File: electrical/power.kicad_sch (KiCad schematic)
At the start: 58 parts

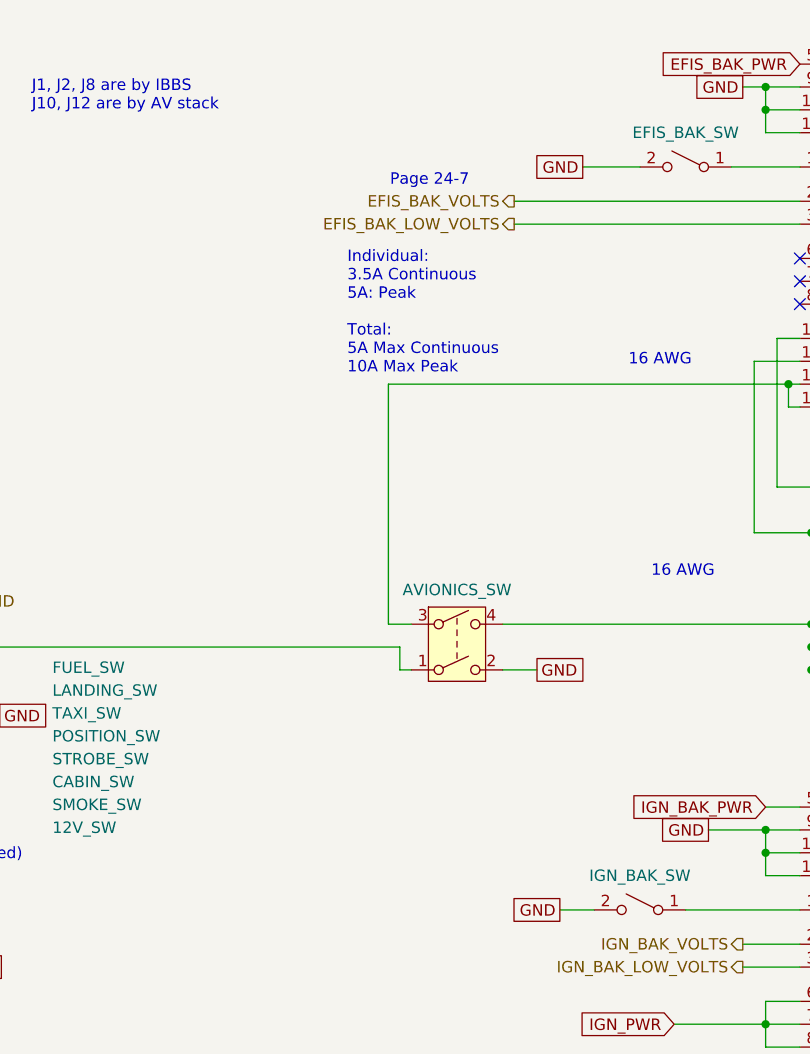
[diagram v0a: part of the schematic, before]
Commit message: Added switch numbers.
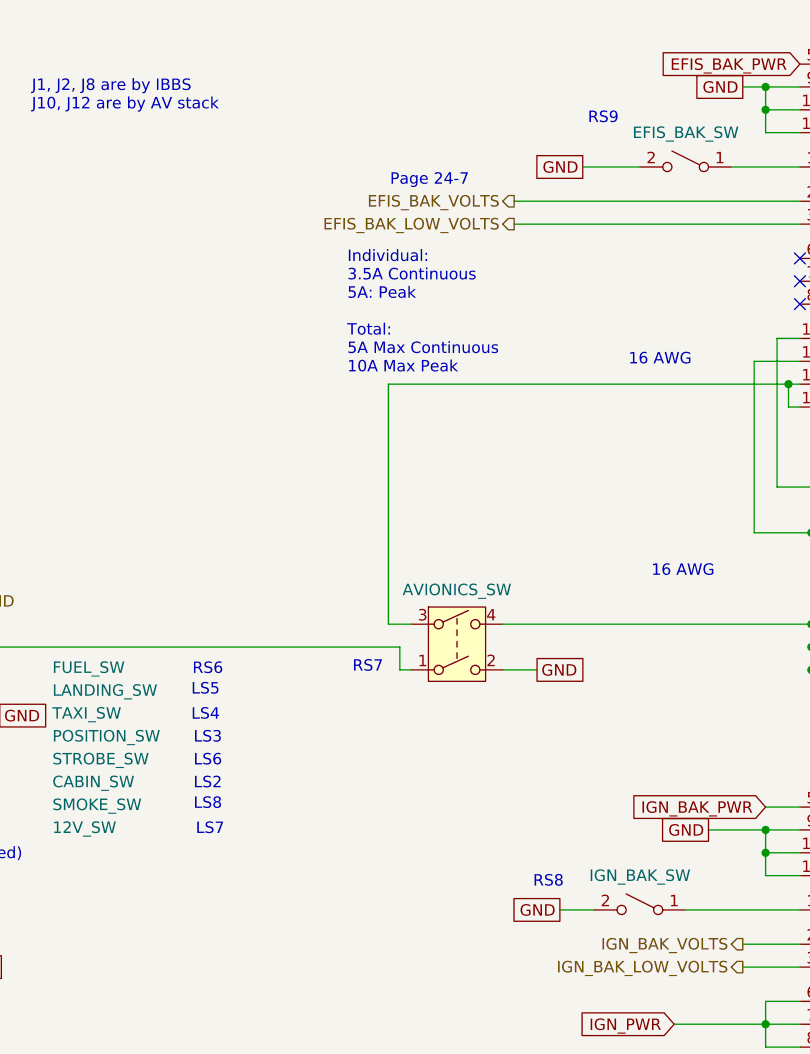
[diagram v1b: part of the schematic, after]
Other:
- note added: "LS2"
- note added: "LS3"
- note added: "LS4"
- note added: "LS5"
- note added: "LS6"
- note added: "LS7"
- note added: "LS8"
- note added: "RS6"
- note added: "RS7"
- note added: "RS8"
- note added: "RS9"
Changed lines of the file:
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@@
 	(title_block
 		(title "Power Distribution")
-		(date "2025-10-01")
-		(rev "1.1.2")
+		(date "2025-10-02")
+		(rev "1.1.3")
 		(company "N78HR")
 	)
@@
 		)
 	)
+	(text "RS8"
+		(exclude_from_sim no)
+		(at 138.43 108.712 0)
+		(effects
+			(font
+				(size 1.27 1.27)
+			)
+		)
+	)
 	(text "Power/Ground 20 AWG\nSignals 22 AWG\nUnless Noted"
 		(exclude_from_sim no)
@@
 		)
 	)
+	(text "RS6"
+		(exclude_from_sim no)
+		(at 100.584 85.09 0)
+		(effects
+			(font
+				(size 1.27 1.27)
+			)
+		)
+	)
 	(text "2A"
 		(exclude_from_sim no)
@@
 		)
 	)
+	(text "LS3"
+		(exclude_from_sim no)
+		(at 100.584 92.71 0)
+		(effects
+			(font
+				(size 1.27 1.27)
+			)
+		)
+	)
 	(text "Backup"
 		(exclude_from_sim no)
@@
 		)
 	)
+	(text "LS4"
+		(exclude_from_sim no)
+		(at 100.33 90.17 0)
+		(effects
+			(font
+				(size 1.27 1.27)
+			)
+		)
+	)
 	(text "16 AWG"
 		(exclude_from_sim no)
@@
 		)
 	)
+	(text "LS7"
+		(exclude_from_sim no)
+		(at 100.838 102.87 0)
+		(effects
+			(font
+				(size 1.27 1.27)
+			)
+		)
+	)
+	(text "RS9"
+		(exclude_from_sim no)
+		(at 144.526 23.876 0)
+		(effects
+			(font
+				(size 1.27 1.27)
+			)
+		)
+	)
 	(text "14 AWG"
 		(exclude_from_sim no)
@@
 		)
 	)
+	(text "LS5"
+		(exclude_from_sim no)
+		(at 100.33 87.376 0)
+		(effects
+			(font
+				(size 1.27 1.27)
+			)
+		)
+	)
 	(text "16 AWG"
 		(exclude_from_sim no)
@@
 		)
 	)
+	(text "LS2"
+		(exclude_from_sim no)
+		(at 100.584 97.79 0)
+		(effects
+			(font
+				(size 1.27 1.27)
+			)
+		)
+	)
 	(text "13A"
 		(exclude_from_sim no)
@@
 		)
 	)
+	(text "RS7"
+		(exclude_from_sim no)
+		(at 118.364 84.836 0)
+		(effects
+			(font
+				(size 1.27 1.27)
+			)
+		)
+	)
 	(text "5A"
 		(exclude_from_sim no)
@@
 		)
 	)
+	(text "LS8"
+		(exclude_from_sim no)
+		(at 100.584 100.076 0)
+		(effects
+			(font
+				(size 1.27 1.27)
+			)
+		)
+	)
 	(text "GROUND_BLOCK"
 		(exclude_from_sim no)
@@
 		(effects
 			(font
+				(size 1.27 1.27)
+			)
+		)
+	)
+	(text "LS6"
+		(exclude_from_sim no)
+		(at 100.584 95.25 0)
+		(effects
+			(font

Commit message: Added RS232 and Canbus wiring notation
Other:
- note added: "Black"
- note added: "Blue"
- note added: "Brown"
- note added: "Destination Open Shield"
- note added: "Green"
- note added: "Pink"
- note added: "Purple"
- note added: "Red"
- note added: "White"
- note added: "White/Black"
- note added: "White/Blue"
- note added: "White/Green"
- note added: "White/Grey"
- note added: "White/Orange"
- note added: "White/Purple"
- note added: "White/Yellow"
- note added: "Yellow"
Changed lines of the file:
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@@
 		(title "Power Distribution")
 		(date "2025-10-02")
-		(rev "1.1.3")
+		(rev "1.1.4")
 		(company "N78HR")
 	)
@@
 		)
 	)
+	(text "Destination\nOpen Shield"
+		(exclude_from_sim no)
+		(at 88.9 74.93 0)
+		(effects
+			(font
+				(size 1.27 1.27)
+			)
+		)
+	)
 	(text "14 AWG"
 		(exclude_from_sim no)
@@
 		)
 	)
+	(text "Yellow"
+		(exclude_from_sim no)
+		(at 92.456 288.798 0)
+		(effects
+			(font
+				(size 1.27 1.27)
+			)
+		)
+	)
 	(text "16 AWG"
 		(exclude_from_sim no)
@@
 		)
 	)
+	(text "Pink"
+		(exclude_from_sim no)
+		(at 92.456 291.084 0)
+		(effects
+			(font
+				(size 1.27 1.27)
+			)
+		)
+	)
 	(text "Pitot Heat (Reserved)"
 		(exclude_from_sim no)
@@
 		)
 	)
+	(text "White/Grey"
+		(exclude_from_sim no)
+		(at 17.78 293.116 0)
+		(effects
+			(font
+				(size 1.27 1.27)
+			)
+		)
+	)
+	(text "White/Purple"
+		(exclude_from_sim no)
+		(at 19.304 285.75 0)
+		(effects
+			(font
+				(size 1.27 1.27)
+			)
+		)
+	)
 	(text "14 AWG"
 		(exclude_from_sim no)
@@
 		)
 	)
+	(text "Blue"
+		(exclude_from_sim no)
+		(at 91.44 280.416 0)
+		(effects
+			(font
+				(size 1.27 1.27)
+			)
+		)
+	)
 	(text "14 AWG"
 		(exclude_from_sim no)
@@
 		)
 	)
+	(text "White/Black"
+		(exclude_from_sim no)
+		(at 19.558 278.13 0)
+		(effects
+			(font
+				(size 1.27 1.27)
+			)
+		)
+	)
 	(text "RS7"
 		(exclude_from_sim no)
@@
 		)
 	)
+	(text "White"
+		(exclude_from_sim no)
+		(at 92.71 296.418 0)
+		(effects
+			(font
+				(size 1.27 1.27)
+			)
+		)
+	)
 	(text "15A"
 		(exclude_from_sim no)
@@
 		)
 	)
+	(text "Purple"
+		(exclude_from_sim no)
+		(at 92.456 286.258 0)
+		(effects
+			(font
+				(size 1.27 1.27)
+			)
+		)
+	)
 	(text "2A"
 		(exclude_from_sim no)
@@
 		)
 	)
+	(text "Brown"
+		(exclude_from_sim no)
+		(at 92.456 293.624 0)
+		(effects
+			(font
+				(size 1.27 1.27)
+			)
+		)
+	)
+	(text "White/Blue"
+		(exclude_from_sim no)
+		(at 19.05 280.416 0)
+		(effects
+			(font
+				(size 1.27 1.27)
+			)
+		)
+	)
+	(text "Red"
+		(exclude_from_sim no)
+		(at 92.456 298.958 0)
+		(effects
+			(font
+				(size 1.27 1.27)
+			)
+		)
+	)
+	(text "Green"
+		(exclude_from_sim no)
+		(at 92.202 283.21 0)
+		(effects
+			(font
+				(size 1.27 1.27)
+			)
+		)
+	)
 	(text "Avionics\nBackup"
 		(exclude_from_sim no)
@@
 		)
 	)
+	(text "White/Yellow"
+		(exclude_from_sim no)
+		(at 19.05 288.29 0)
+		(effects
+			(font
+				(size 1.27 1.27)
+			)
+		)
+	)
+	(text "White/Orange"
+		(exclude_from_sim no)
+		(at 19.05 290.83 0)
+		(effects
+			(font
+				(size 1.27 1.27)
+			)
+		)
+	)
 	(text "5A"
 		(exclude_from_sim no)
@@
 		)
 	)
+	(text "Black"
+		(exclude_from_sim no)
+		(at 91.694 277.876 0)
+		(effects
+			(font
+				(size 1.27 1.27)
+			)
+		)
+	)
 	(text "5A"
 		(exclude_from_sim no)
@@
 		(effects
 			(font
+				(size 1.27 1.27)
+			)
+		)
+	)
+	(text "White"
+		(exclude_from_sim no)
+		(at 18.034 295.402 0)
+		(effects
+			(font
+				(size 1.27 1.27)
+			)
+		)
+	)
+	(text "White/Green"
+		(exclude_from_sim no)
+		(at 19.558 282.956 0)
+		(effects
+			(font

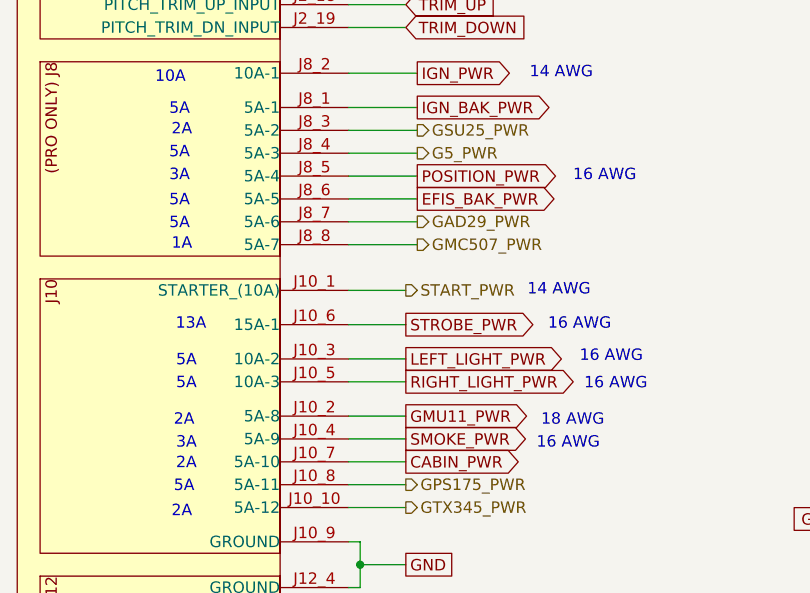
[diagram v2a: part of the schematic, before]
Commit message: Added colors to GTP 59 symbol. Moved power around as best as I could to accomodate lights together.
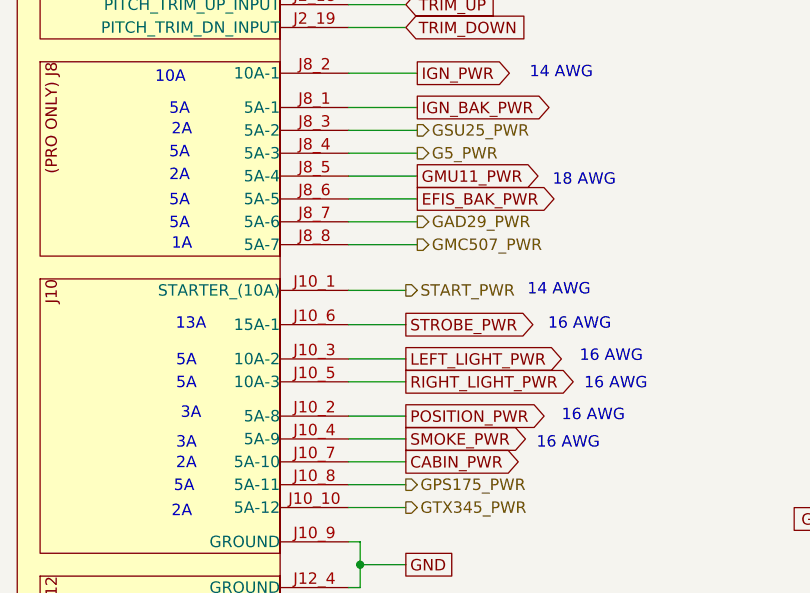
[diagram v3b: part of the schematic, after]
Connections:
- net GMU11_PWR: now also VPX.J8_5 (5A-4); no longer VPX.J10_2 (5A-8)
- net POSITION_PWR: now also VPX.J10_2 (5A-8); no longer VPX.J8_5 (5A-4)
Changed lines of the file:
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@@
 	(title_block
 		(title "Power Distribution")
-		(date "2025-10-02")
-		(rev "1.1.4")
+		(date "2025-10-12")
+		(rev "1.1.8")
 		(company "N78HR")
 	)
@@
 	(text "16 AWG"
 		(exclude_from_sim no)
-		(at 85.598 144.78 0)
+		(at 84.328 171.45 0)
 		(effects
 			(font
@@
 	(text "18 AWG"
 		(exclude_from_sim no)
-		(at 82.042 171.958 0)
+		(at 83.312 145.288 0)
 		(effects
 			(font
@@
 	(text "2A"
 		(exclude_from_sim no)
-		(at 38.862 171.958 0)
+		(at 38.354 144.78 0)
 		(effects
 			(font
@@
 	(text "3A"
 		(exclude_from_sim no)
-		(at 38.354 144.78 0)
+		(at 39.624 171.196 0)
 		(effects
 			(font
@@
 	(wire
 		(pts
-			(xy 57.15 171.45) (xy 63.5 171.45)
-		)
-		(stroke
-			(width 0)
-			(type default)
-		)
-	)
-	(wire
-		(pts
 			(xy 116.84 347.98) (xy 116.84 350.52)
 		)
@@
 	(wire
 		(pts
-			(xy 57.15 144.78) (xy 64.77 144.78)
-		)
-		(stroke
-			(width 0)
-			(type default)
-		)
-	)
-	(wire
-		(pts
 			(xy 57.15 128.27) (xy 63.5 128.27)
 		)
@@
 	(wire
 		(pts
+			(xy 57.15 144.78) (xy 64.77 144.78)
+		)
+		(stroke
+			(width 0)
+			(type default)
+		)
+	)
+	(wire
+		(pts
 			(xy 180.34 153.67) (xy 180.34 149.86)
 		)
@@
 	(wire
 		(pts
+			(xy 57.15 176.53) (xy 63.5 176.53)
+		)
+		(stroke
+			(width 0)
+			(type default)
+		)
+	)
+	(wire
+		(pts
 			(xy 68.58 339.09) (xy 68.58 336.55)
 		)
@@
 	(wire
 		(pts
-			(xy 57.15 173.99) (xy 63.5 173.99)
-		)
-		(stroke
-			(width 0)
-			(type default)
-		)
-	)
-	(wire
-		(pts
 			(xy 68.58 298.45) (xy 69.85 298.45)
 		)
@@
 	(wire
 		(pts
-			(xy 139.7 111.76) (xy 143.51 111.76)
+			(xy 57.15 171.45) (xy 63.5 171.45)
 		)
 		(stroke
@@
 	(wire
 		(pts
-			(xy 165.1 53.34) (xy 166.37 53.34)
+			(xy 139.7 111.76) (xy 143.51 111.76)
 		)
 		(stroke
@@
 	(wire
 		(pts
-			(xy 57.15 142.24) (xy 64.77 142.24)
+			(xy 165.1 53.34) (xy 166.37 53.34)
 		)
 		(stroke
@@
 	(wire
 		(pts
-			(xy 80.01 334.01) (xy 102.87 334.01)
+			(xy 57.15 142.24) (xy 64.77 142.24)
 		)
 		(stroke
@@
 	(wire
 		(pts
-			(xy 57.15 176.53) (xy 63.5 176.53)
+			(xy 80.01 334.01) (xy 102.87 334.01)
 		)
 		(stroke
@@
 	(wire
 		(pts
+			(xy 57.15 173.99) (xy 63.5 173.99)
+		)
+		(stroke
+			(width 0)
+			(type default)
+		)
+	)
+	(wire
+		(pts
 			(xy 57.15 90.17) (xy 62.23 90.17)
 		)
@@
 	(global_label "GMU11_PWR"
 		(shape output)
-		(at 63.5 171.45 0)
+		(at 64.77 144.78 0)
 		(fields_autoplaced yes)
 		(effects
@@
 		)
 		(property "Intersheetrefs" "${INTERSHEET_REFS}"
-			(at 77.9151 171.45 0)
+			(at 79.1851 144.78 0)
 			(effects
 				(font
@@
 	(global_label "POSITION_PWR"
 		(shape output)
-		(at 64.77 144.78 0)
+		(at 63.5 171.45 0)
 		(fields_autoplaced yes)
 		(effects
@@
 		)
 		(property "Intersheetrefs" "${INTERSHEET_REFS}"
-			(at 81.3624 144.78 0)
+			(at 80.0924 171.45 0)
 			(effects
 				(font
